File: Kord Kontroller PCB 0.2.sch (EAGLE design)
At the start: 187 parts, among them IC2 74HCT1G125DBV, J1 MIDIOUTB, J2 MIDIOUTA, J3 FTSH-105-01-L-DV-KJ, SW2 SPST_TACT-KMR2, U1 AP2112K-3.3, U2 ATSAMD51J19A-AUT, X3 microUSB

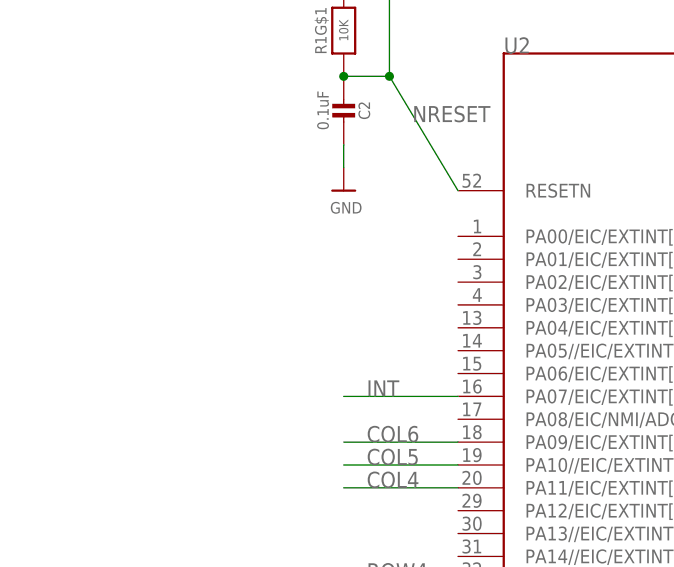
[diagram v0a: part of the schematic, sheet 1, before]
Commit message: Added osc and reourting diodes
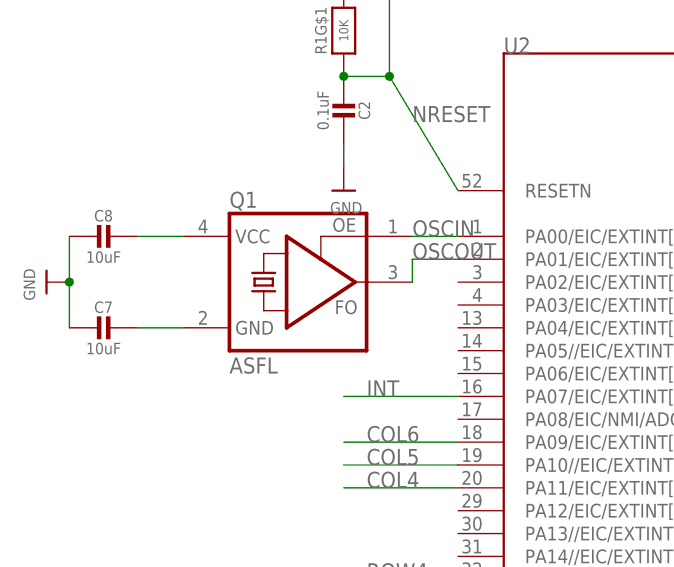
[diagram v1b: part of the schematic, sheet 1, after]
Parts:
- added C7, C8: 10uF, microbuilder:CAP_CERAMIC0805-NOOUTLINE
- added Q1: ASFL, crystal:ASFL
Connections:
- new net N$63: C8.1, Q1.VCC
- new net N$69: C7.1, Q1.GND
- new net OSCIN: Q1.OE, U2.PA00/EIC/EXTINT[0]
- new net OSCOUT: Q1.FO, U2.PA01/EIC/EXTINT[1]
- net GND: now also C7.2, C8.2
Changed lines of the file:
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@@
 <part name="D29" library="microbuilder" deviceset="DIODE" device="SOD-323" value="1N4148"/>
 <part name="B29" library="microbuilder" deviceset="ELAST_10X10" device=""/>
+<part name="U$8" library="microbuilder" deviceset="GND" device=""/>
+<part name="C7" library="microbuilder" deviceset="CAP_CERAMIC" device="0805-NOOUTLINE" value="10uF"/>
+<part name="C8" library="microbuilder" deviceset="CAP_CERAMIC" device="0805-NOOUTLINE" value="10uF"/>
+<part name="Q1" library="crystal" library_urn="urn:adsk.eagle:library:204" deviceset="ASF*" device="" package3d_urn="urn:adsk.eagle:package:12096/1" technology="L"/>
 </parts>
 <sheets>
@@
 <attribute name="VALUE" x="803.656" y="-75.184" size="1.27" layer="96"/>
 </instance>
+<instance part="U$8" gate="G$1" x="619.76" y="-27.94" smashed="yes" rot="R270">
+<attribute name="VALUE" x="617.22" y="-26.416" size="1.27" layer="96" rot="R270"/>
+</instance>
+<instance part="C7" gate="G$1" x="624.84" y="-33.02" smashed="yes" rot="R270">
+<attribute name="NAME" x="626.09" y="-30.73" size="1.27" layer="95" font="vector" align="center"/>
+<attribute name="VALUE" x="626.09" y="-35.32" size="1.27" layer="96" font="vector" align="center"/>
+</instance>
+<instance part="C8" gate="G$1" x="624.84" y="-22.86" smashed="yes" rot="R270">
+<attribute name="NAME" x="626.09" y="-20.57" size="1.27" layer="95" font="vector" align="center"/>
+<attribute name="VALUE" x="626.09" y="-25.16" size="1.27" layer="96" font="vector" align="center"/>
+</instance>
+<instance part="Q1" gate="G$1" x="647.7" y="-27.94" smashed="yes">
+<attribute name="NAME" x="640.08" y="-19.685" size="1.778" layer="95"/>
+<attribute name="VALUE" x="640.08" y="-38.1" size="1.778" layer="96"/>
+</instance>
 </instances>
 <busses>
@@
 <pinref part="U2" gate="G$1" pin="GND"/>
 <wire x1="779.78" y1="-91.44" x2="777.24" y2="-91.44" width="0.1524" layer="91"/>
+</segment>
+<segment>
+<pinref part="U$8" gate="G$1" pin="GND"/>
+<pinref part="C7" gate="G$1" pin="2"/>
+<wire x1="622.3" y1="-27.94" x2="622.3" y2="-33.02" width="0.1524" layer="91"/>
+<wire x1="622.3" y1="-27.94" x2="622.3" y2="-22.86" width="0.1524" layer="91"/>
+<junction x="622.3" y="-27.94"/>
+<pinref part="C8" gate="G$1" pin="2"/>
 </segment>
 </net>
@@
 </segment>
 </net>
+<net name="N$63" class="0">
+<segment>
+<pinref part="C8" gate="G$1" pin="1"/>
+<pinref part="Q1" gate="G$1" pin="VCC"/>
+<wire x1="629.92" y1="-22.86" x2="635" y2="-22.86" width="0.1524" layer="91"/>
+</segment>
+</net>
+<net name="N$69" class="0">
+<segment>
+<pinref part="C7" gate="G$1" pin="1"/>
+<pinref part="Q1" gate="G$1" pin="GND"/>
+<wire x1="629.92" y1="-33.02" x2="635" y2="-33.02" width="0.1524" layer="91"/>
+</segment>
+</net>
+<net name="OSCIN" class="0">
+<segment>
+<pinref part="Q1" gate="G$1" pin="OE"/>
+<pinref part="U2" gate="G$1" pin="PA00/EIC/EXTINT[0]"/>
+<wire x1="660.4" y1="-22.86" x2="665.48" y2="-22.86" width="0.1524" layer="91"/>
+<label x="660.4" y="-22.86" size="1.778" layer="95"/>
+</segment>
+</net>
+<net name="OSCOUT" class="0">
+<segment>
+<pinref part="Q1" gate="G$1" pin="FO"/>
+<pinref part="U2" gate="G$1" pin="PA01/EIC/EXTINT[1]"/>
+<wire x1="660.4" y1="-27.94" x2="660.4" y2="-25.4" width="0.1524" layer="91"/>
+<wire x1="660.4" y1="-25.4" x2="665.48" y2="-25.4" width="0.1524" layer="91"/>
+<label x="660.4" y="-25.4" size="1.778" layer="95"/>
+</segment>
+</net>

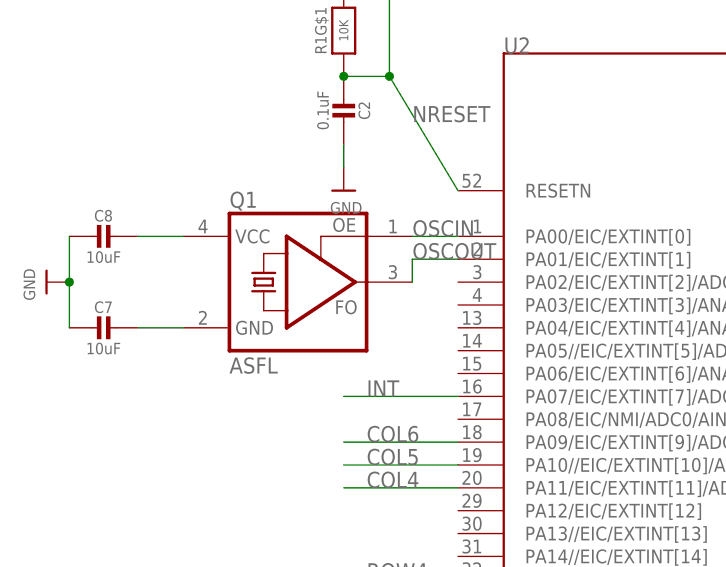
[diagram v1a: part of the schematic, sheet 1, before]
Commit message: Moved resistors to bottom and Added 32k crystal
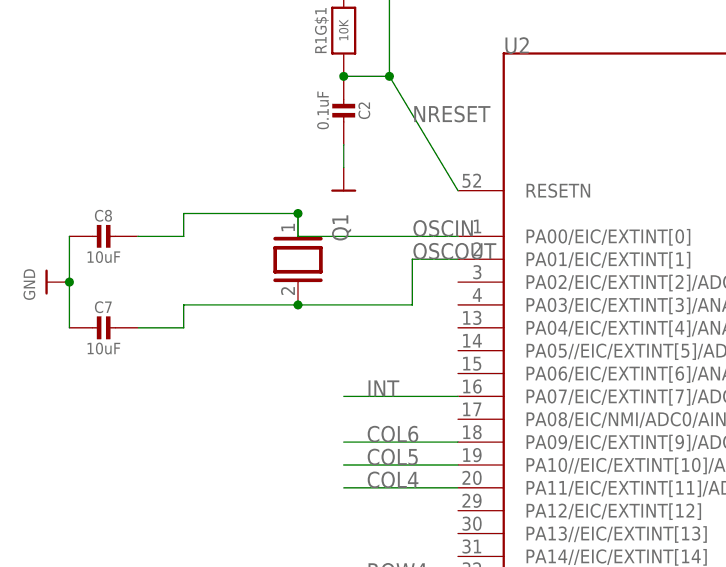
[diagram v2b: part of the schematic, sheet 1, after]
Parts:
- Q1: value ASFL -> (none); device crystal:ASFL -> special:XTAL/S
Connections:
- removed net N$63: C8.1, Q1.VCC
- removed net N$69: C7.1, Q1.GND
- net OSCIN: now also C8.1, Q1.1; no longer Q1.OE
- net OSCOUT: now also C7.1, Q1.2; no longer Q1.FO
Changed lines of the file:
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@@
 <part name="C7" library="microbuilder" deviceset="CAP_CERAMIC" device="0805-NOOUTLINE" value="10uF"/>
 <part name="C8" library="microbuilder" deviceset="CAP_CERAMIC" device="0805-NOOUTLINE" value="10uF"/>
-<part name="Q1" library="crystal" library_urn="urn:adsk.eagle:library:204" deviceset="ASF*" device="" package3d_urn="urn:adsk.eagle:package:12096/1" technology="L"/>
+<part name="Q1" library="special" library_urn="urn:adsk.eagle:library:367" deviceset="XTAL/S" device="" package3d_urn="urn:adsk.eagle:package:26647/2"/>
 </parts>
 <sheets>
@@
 <attribute name="VALUE" x="650.48" y="-8.87" size="1.27" layer="96" font="vector" rot="R270" align="center"/>
 </instance>
-<instance part="U$4" gate="G$1" x="652.78" y="-17.78" smashed="yes">
-<attribute name="VALUE" x="651.256" y="-20.32" size="1.27" layer="96"/>
-</instance>
+<instance part="U$4" gate="G$1" x="652.78" y="-17.78" smashed="yes"/>
 <instance part="U$5" gate="G$1" x="652.78" y="12.7" smashed="yes">
 <attribute name="VALUE" x="651.256" y="13.716" size="1.27" layer="96"/>
@@
 <attribute name="VALUE" x="626.09" y="-25.16" size="1.27" layer="96" font="vector" align="center"/>
 </instance>
-<instance part="Q1" gate="G$1" x="647.7" y="-27.94" smashed="yes">
-<attribute name="NAME" x="640.08" y="-19.685" size="1.778" layer="95"/>
-<attribute name="VALUE" x="640.08" y="-38.1" size="1.778" layer="96"/>
+<instance part="Q1" gate="G$1" x="647.7" y="-25.4" smashed="yes" rot="R270">
+<attribute name="NAME" x="651.51" y="-20.32" size="1.778" layer="95" rot="R270"/>
+<attribute name="VALUE" x="642.62" y="-20.32" size="1.778" layer="96" rot="R270"/>
 </instance>
 </instances>
@@
 </segment>
 </net>
-<net name="N$63" class="0">
-<segment>
+<net name="OSCIN" class="0">
+<segment>
+<pinref part="U2" gate="G$1" pin="PA00/EIC/EXTINT[0]"/>
+<label x="660.4" y="-22.86" size="1.778" layer="95"/>
+<pinref part="Q1" gate="G$1" pin="1"/>
+<wire x1="665.48" y1="-22.86" x2="647.7" y2="-22.86" width="0.1524" layer="91"/>
+<wire x1="647.7" y1="-22.86" x2="647.7" y2="-20.32" width="0.1524" layer="91"/>
 <pinref part="C8" gate="G$1" pin="1"/>
-<pinref part="Q1" gate="G$1" pin="VCC"/>
 <wire x1="629.92" y1="-22.86" x2="635" y2="-22.86" width="0.1524" layer="91"/>
-</segment>
-</net>
-<net name="N$69" class="0">
-<segment>
-<pinref part="C7" gate="G$1" pin="1"/>
-<pinref part="Q1" gate="G$1" pin="GND"/>
-<wire x1="629.92" y1="-33.02" x2="635" y2="-33.02" width="0.1524" layer="91"/>
-</segment>
-</net>
-<net name="OSCIN" class="0">
-<segment>
-<pinref part="Q1" gate="G$1" pin="OE"/>
-<pinref part="U2" gate="G$1" pin="PA00/EIC/EXTINT[0]"/>
-<wire x1="660.4" y1="-22.86" x2="665.48" y2="-22.86" width="0.1524" layer="91"/>
-<label x="660.4" y="-22.86" size="1.778" layer="95"/>
+<wire x1="647.7" y1="-20.32" x2="635" y2="-20.32" width="0.1524" layer="91"/>
+<wire x1="635" y1="-20.32" x2="635" y2="-22.86" width="0.1524" layer="91"/>
+<junction x="647.7" y="-20.32"/>
 </segment>
 </net>
 <net name="OSCOUT" class="0">
 <segment>
-<pinref part="Q1" gate="G$1" pin="FO"/>
 <pinref part="U2" gate="G$1" pin="PA01/EIC/EXTINT[1]"/>
-<wire x1="660.4" y1="-27.94" x2="660.4" y2="-25.4" width="0.1524" layer="91"/>
+<wire x1="660.4" y1="-30.48" x2="660.4" y2="-25.4" width="0.1524" layer="91"/>
 <wire x1="660.4" y1="-25.4" x2="665.48" y2="-25.4" width="0.1524" layer="91"/>
 <label x="660.4" y="-25.4" size="1.778" layer="95"/>
-</segment>
-</net>
+<pinref part="Q1" gate="G$1" pin="2"/>
+<wire x1="660.4" y1="-30.48" x2="647.7" y2="-30.48" width="0.1524" layer="91"/>
+<pinref part="C7" gate="G$1" pin="1"/>
+<wire x1="629.92" y1="-33.02" x2="635" y2="-33.02" width="0.1524" layer="91"/>
+<wire x1="647.7" y1="-30.48" x2="635" y2="-30.48" width="0.1524" layer="91"/>
+<wire x1="635" y1="-30.48" x2="635" y2="-33.02" width="0.1524" layer="91"/>
+<junction x="647.7" y="-30.48"/>
+</segment>
+</net>

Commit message: moved some stuff around
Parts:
- Q1: value (none) -> 32kHz
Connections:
- removed net AVDD: U2.VDDANA
- removed net INT: U2.PA07/EIC/EXTINT[7]/ADC0/AIN[7]
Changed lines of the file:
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@@
 <part name="U$1" library="microbuilder" deviceset="GND" device=""/>
 <part name="C1" library="microbuilder" deviceset="CAP_CERAMIC" device="0805-NOOUTLINE" value="10uF"/>
-<part name="U$2" library="microbuilder" deviceset="AVDD" device=""/>
 <part name="GND3" library="supply1" deviceset="GND" device=""/>
 <part name="SW2" library="adafruit" deviceset="SPST_TACT" device="-KMR2"/>
@@
 <part name="C7" library="microbuilder" deviceset="CAP_CERAMIC" device="0805-NOOUTLINE" value="10uF"/>
 <part name="C8" library="microbuilder" deviceset="CAP_CERAMIC" device="0805-NOOUTLINE" value="10uF"/>
-<part name="Q1" library="special" library_urn="urn:adsk.eagle:library:367" deviceset="XTAL/S" device="" package3d_urn="urn:adsk.eagle:package:26647/2"/>
+<part name="Q1" library="special" library_urn="urn:adsk.eagle:library:367" deviceset="XTAL/S" device="" package3d_urn="urn:adsk.eagle:package:26647/2" value="32kHz"/>
 </parts>
 <sheets>
@@
 <attribute name="VALUE" x="782.56" y="1.29" size="1.27" layer="96" font="vector" rot="R270" align="center"/>
 </instance>
-<instance part="U$2" gate="G$1" x="789.94" y="-5.08" smashed="yes"/>
 <instance part="GND3" gate="1" x="708.66" y="2.54" smashed="yes">
 <attribute name="VALUE" x="706.12" y="0" size="1.778" layer="96"/>
@@
 <junction x="622.3" y="-27.94"/>
 <pinref part="C8" gate="G$1" pin="2"/>
-</segment>
-</net>
-<net name="INT" class="0">
-<segment>
-<wire x1="652.78" y1="-40.64" x2="665.48" y2="-40.64" width="0.1524" layer="91"/>
-<label x="655.32" y="-40.64" size="1.778" layer="95"/>
-<pinref part="U2" gate="G$1" pin="PA07/EIC/EXTINT[7]/ADC0/AIN[7]"/>
 </segment>
 </net>
@@
 </segment>
 </net>
-<net name="AVDD" class="0">
-<segment>
-<wire x1="777.24" y1="-7.62" x2="789.94" y2="-7.62" width="0.1524" layer="91"/>
-<pinref part="U$2" gate="G$1" pin="AVDD"/>
-<pinref part="U2" gate="G$1" pin="VDDANA"/>
-</segment>
-</net>

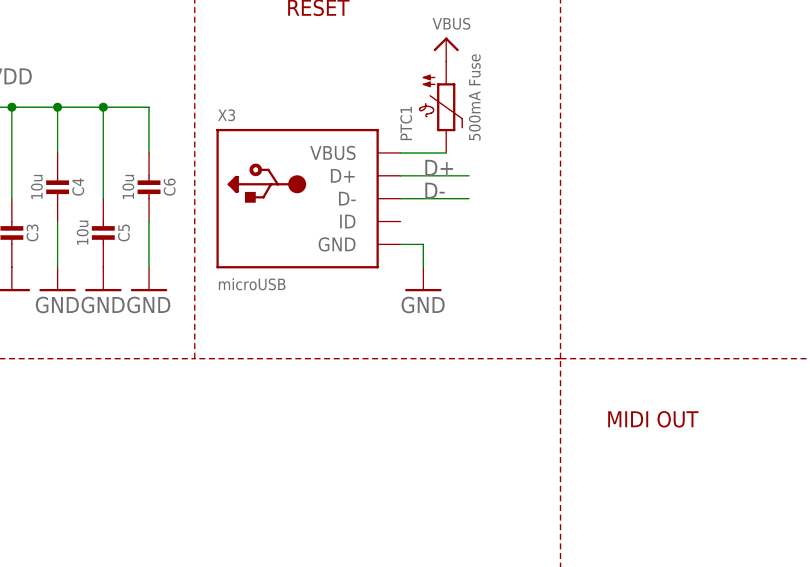
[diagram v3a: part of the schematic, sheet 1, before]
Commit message: Rotated LEDs to remove DRC errors
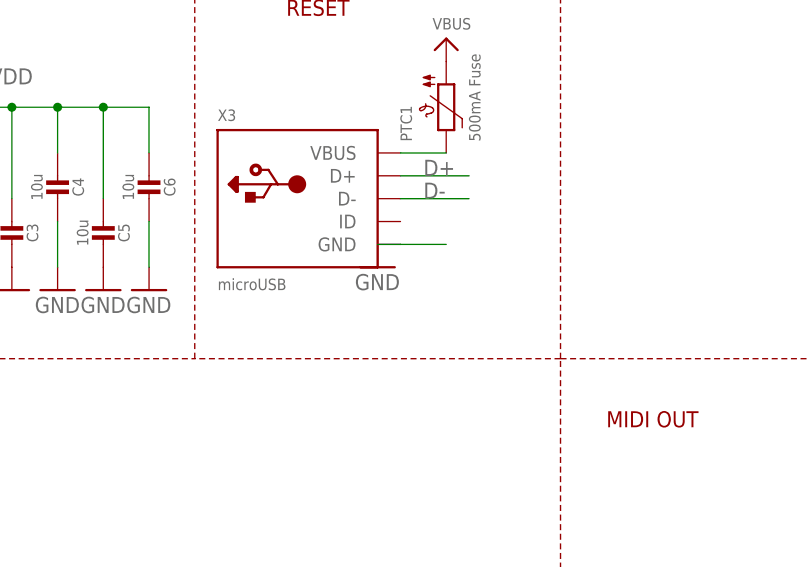
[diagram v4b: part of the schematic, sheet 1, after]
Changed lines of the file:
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@@
 <attribute name="VALUE" x="656.336" y="111.76" size="1.27" layer="96"/>
 </instance>
-<instance part="GND14" gate="1" x="759.46" y="114.3" smashed="yes">
-<attribute name="VALUE" x="756.92" y="111.76" size="1.778" layer="96"/>
+<instance part="GND14" gate="1" x="754.38" y="116.84" smashed="yes">
+<attribute name="VALUE" x="751.84" y="114.3" size="1.778" layer="96"/>
 </instance>
 <instance part="U$56" gate="G$1" x="762" y="142.24" smashed="yes">
@@
 </segment>
 <segment>
-<wire x1="756.92" y1="119.38" x2="759.46" y2="119.38" width="0.1524" layer="91"/>
-<wire x1="759.46" y1="119.38" x2="759.46" y2="116.84" width="0.1524" layer="91"/>
+<wire x1="756.92" y1="119.38" x2="762" y2="119.38" width="0.1524" layer="91"/>
+<wire x1="756.92" y1="119.38" x2="754.38" y2="119.38" width="0.1524" layer="91"/>
 <pinref part="GND14" gate="1" pin="GND"/>
 <pinref part="X3" gate="G$1" pin="GND"/>
@@
 <segment>
 <pinref part="X3" gate="G$1" pin="D-"/>
+<label x="759.46" y="124.46" size="1.778" layer="95"/>
 <wire x1="764.54" y1="124.46" x2="756.92" y2="124.46" width="0.1524" layer="91"/>
-<label x="759.46" y="124.46" size="1.778" layer="95"/>
-</segment>
-<segment>
+</segment>
+<segment>
